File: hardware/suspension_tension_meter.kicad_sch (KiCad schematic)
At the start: 19 parts, among them J1 Goldpin, J2 24V, J3 CAN, U1 STM32L4P5RET6, Y1 TBD

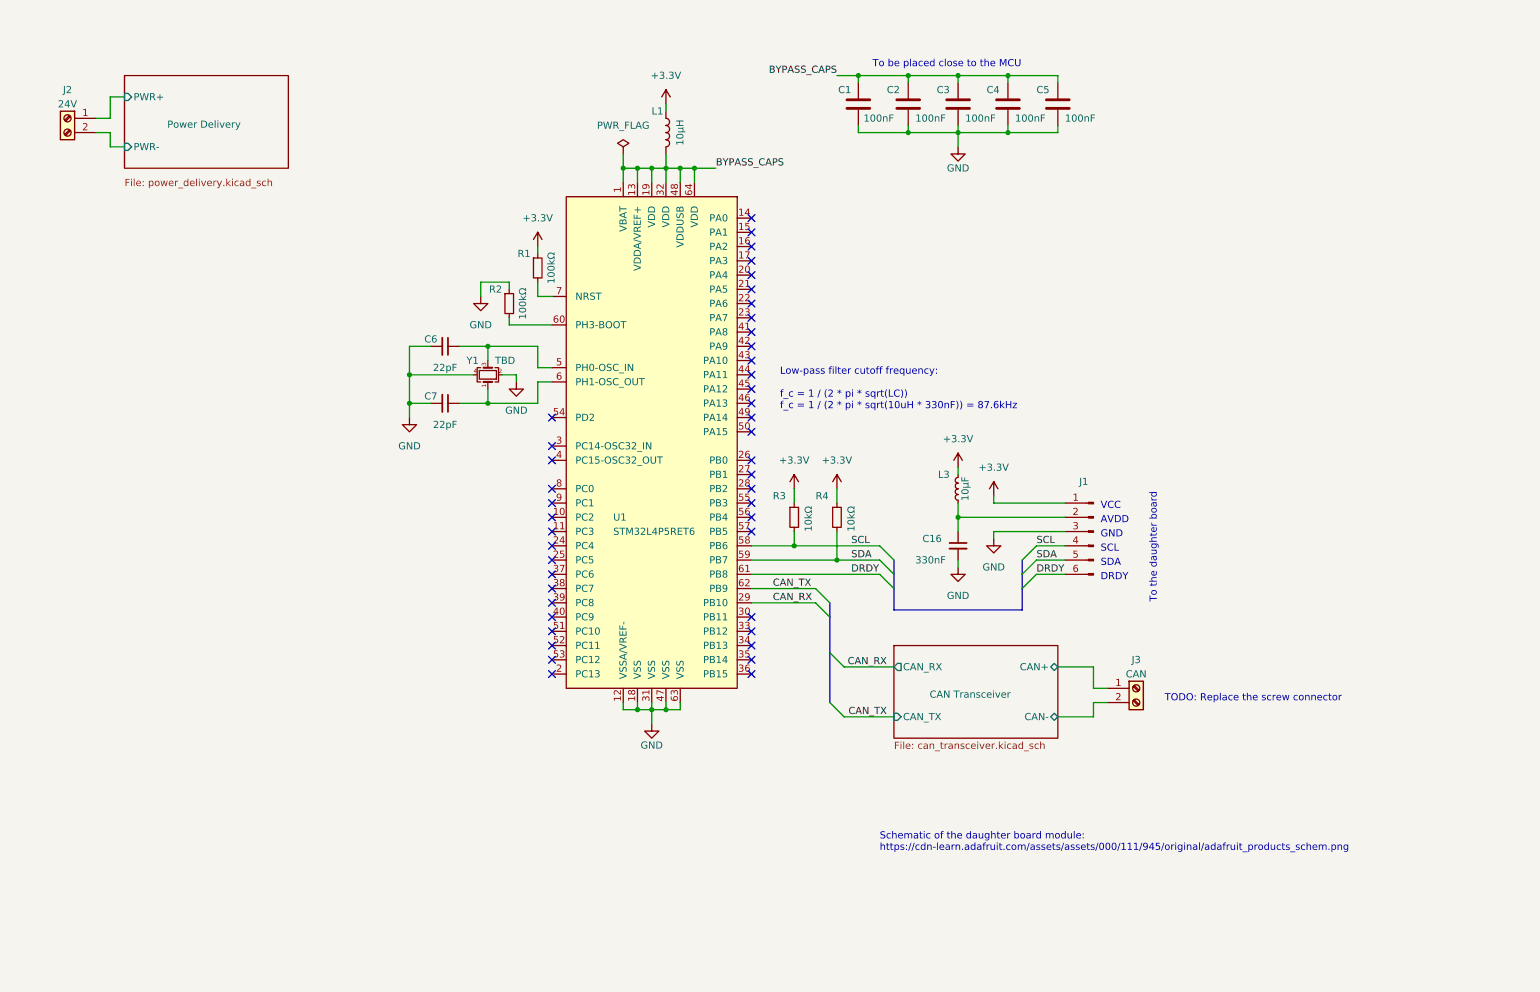
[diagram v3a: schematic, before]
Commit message: Refactor the main sheet
- Replace screw connectors with a goldpin header
- Add reset button
- Add SWD debugger header
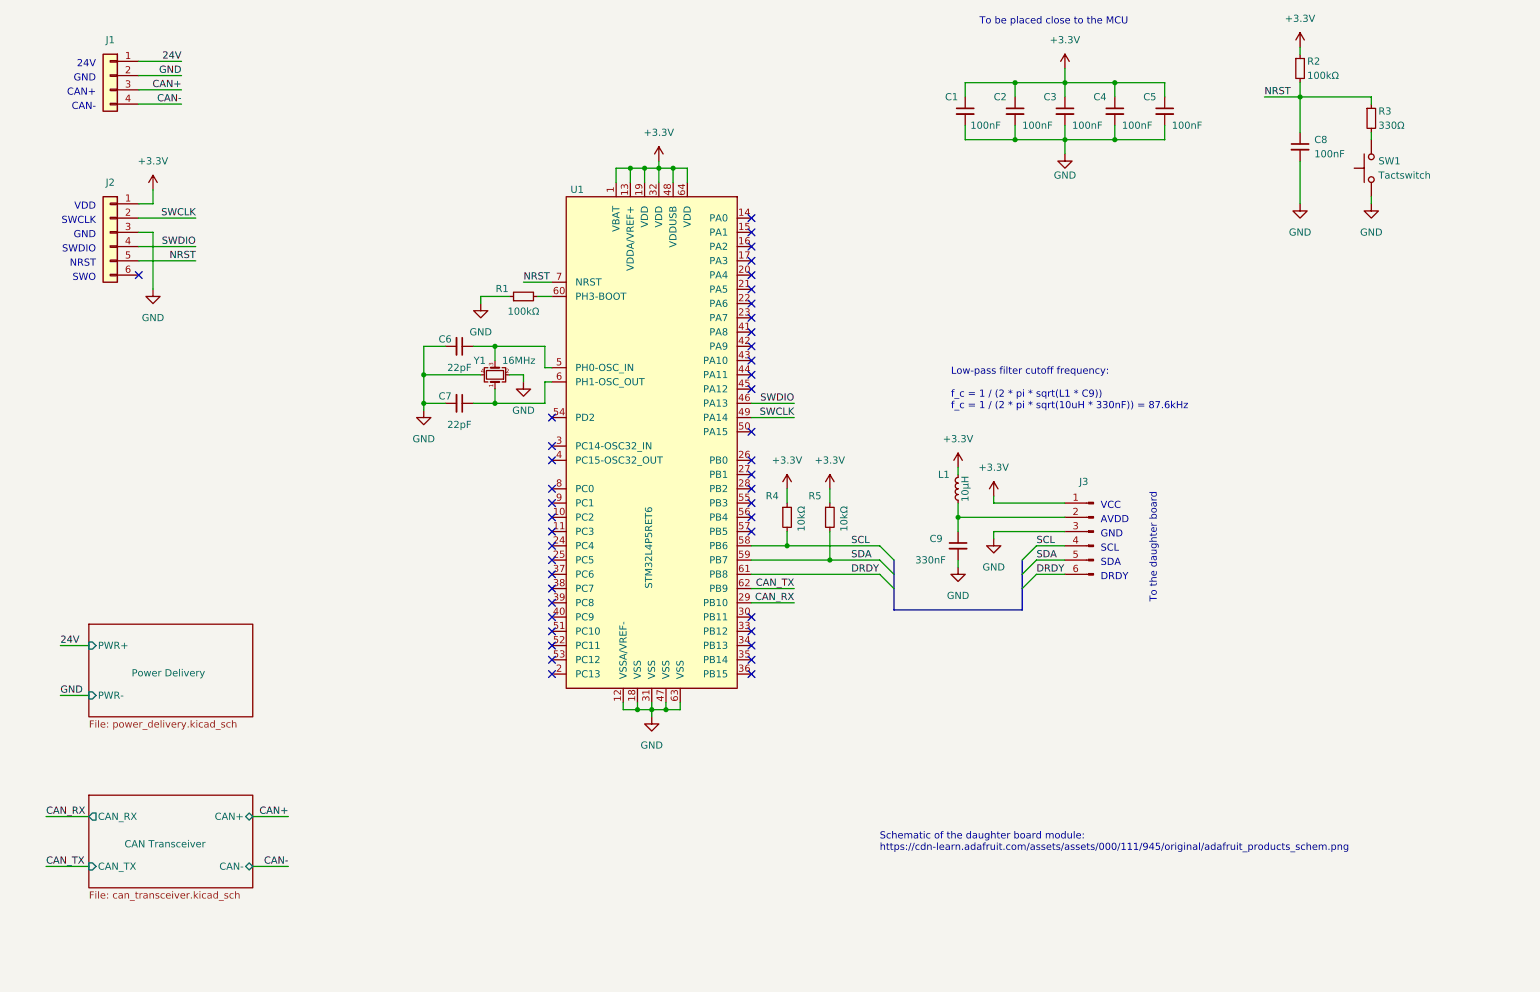
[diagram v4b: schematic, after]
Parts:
- removed J2: 24V, symbol Connector:Screw_Terminal_01x02
- removed J3: CAN, symbol Connector:Screw_Terminal_01x02
- removed L1: 10μH, Inductor_SMD:L_0805_2012Metric, symbol Device:L
- removed R1: 100kΩ, Resistor_SMD:R_0603_1608Metric, symbol Device:R_Small
- added C8: 100nF, symbol Device:C_Small
- added J1: Conn_01x04, symbol Connector_Generic:Conn_01x04
- added J2: Conn_01x06, symbol Connector_Generic:Conn_01x06
- added R2: 100kΩ, symbol Device:R_Small
- added R3: 330Ω, symbol Device:R_Small
- added SW1: Tactswitch, symbol Switch:SW_Push
- C1, C2, C3, C4, C5: symbol Device:C -> Device:C_Small
- L1: renamed from L3; value 10μF -> 10μH
- Y1: value TBD -> 16MHz
- renumbered C16 to C9, J1 to J3, R2 to R1, R3 to R4, R4 to R5
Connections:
- net BYPASS_CAPS is gone; now on net +3.3V: C1.1, C2.1, C3.1, C4.1, C5.1, U1.1 (VBAT), U1.13 (VDDA/VREF+), U1.19 (VDD), U1.32 (VDD), U1.48 (VDDUSB), U1.64 (VDD)
- net +3.3V: now also J2.1 (Pin_1), R2.1
- net GND: now also C8.2, J1.2 (Pin_2), J2.3 (Pin_3), SW1.1
- net SWDIO: now reaches U1.46 (PA13)
- net SWDIO: now also J2.4 (Pin_4)
- net SWCLK: now reaches U1.49 (PA14)
- net SWCLK: now also J2.2 (Pin_2)
- net NRST: now reaches U1.7 (NRST)
- net NRST: now also C8.1, J2.5 (Pin_5), R2.2, R3.1
- new net: R3.2, SW1.2
- new net 24V: J1.1 (Pin_1)
- new net CAN+: J1.3 (Pin_3)
- new net CAN-: J1.4 (Pin_4)
- no-connect marks 44 -> 43
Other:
- note added: "24V"
- note added: "CAN+"
- note added: "CAN-"
- note added: "Low-pass filter cutoff frequency: f_c = 1 / (2 * pi * sqrt(L1 * C9)) f_c = 1 / (2 * pi * sqrt(10uH * 330nF)) = 87.6kHz"
- note added: "NRST"
- note added: "SWCLK"
- note added: "SWDIO"
- note added: "SWO"
- note added: "VDD"
- note removed: "Low-pass filter cutoff frequency: f_c = 1 / (2 * pi * sqrt(LC)) f_c = 1 / (2 * pi * sqrt(10uH * 330nF)) = 87.6kHz"
- note removed: "TODO: Replace the screw connector"
- moved on the sheet: C1, C2, C3, C4, C5, C6, C7, R1, R4, R5, Y1

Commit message: Add ADC circuit
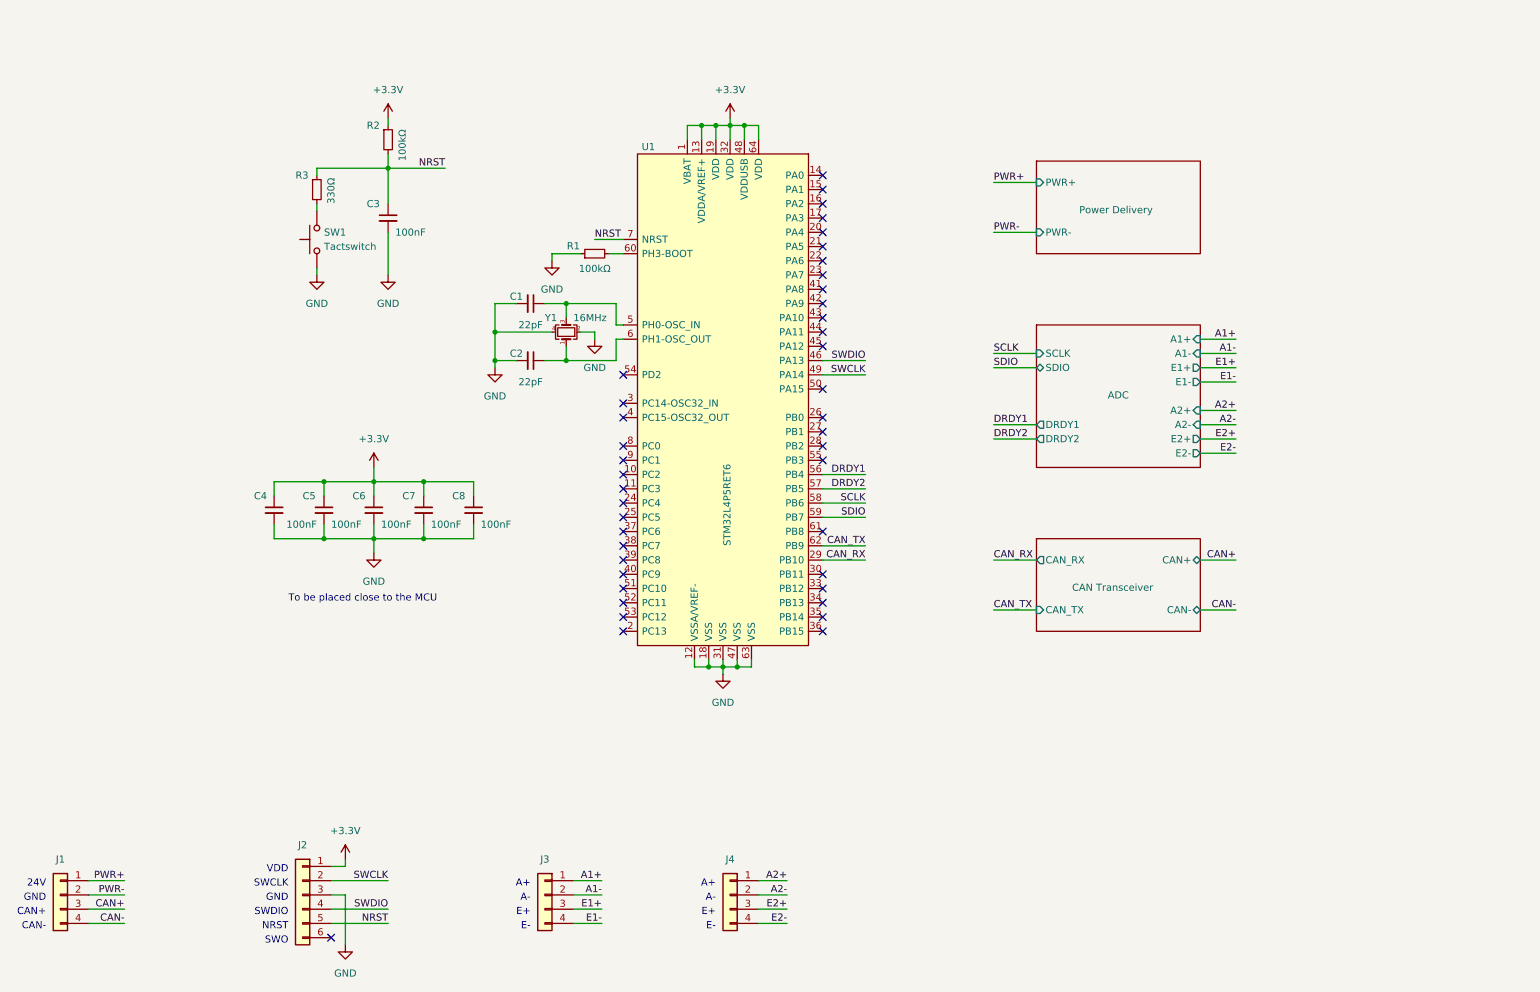
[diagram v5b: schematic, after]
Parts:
- removed C9: 330nF, symbol Device:C_Small
- removed J3: Goldpin, symbol Connector:Conn_01x06_Male
- removed L1: 10μH, symbol Device:L_Small
- removed R4, R5: 10kΩ, symbol Device:R_Small
- added J3, J4: Conn_01x04, symbol Connector_Generic:Conn_01x04
- U1: symbol Local_Library:STM32L4P5RET6-STM32L4P5RET6 -> Local_Library:STM32L4P5RET6
- renumbered C6 to C1, C7 to C2, C8 to C3, C1 to C4, C2 to C5, C3 to C6, C4 to C7, C5 to C8
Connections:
- net GND: no longer J1.2 (Pin_2)
- net DRDY1: now reaches U1.56 (PB4)
- net DRDY2: now reaches U1.57 (PB5)
- net 24V renamed PWR+
- net DRDY: no longer names the net of U1.61 (PB8)
- net SCL renamed SCLK
- net SDA renamed SDIO
- new net A1+: J3.1 (Pin_1)
- new net A1-: J3.2 (Pin_2)
- new net A2+: J4.1 (Pin_1)
- new net A2-: J4.2 (Pin_2)
- new net E1+: J3.3 (Pin_3)
- new net E1-: J3.4 (Pin_4)
- new net E2+: J4.3 (Pin_3)
- new net E2-: J4.4 (Pin_4)
- new net PWR-: J1.2 (Pin_2)
- no-connect marks 43 -> 42
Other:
- added sheet ADC (adc.kicad_sch)
- note added: "A+"
- note added: "A-"
- note added: "E+"
- note added: "E-"
- note removed: "AVDD"
- note removed: "DRDY"
- note removed: "Low-pass filter cutoff frequency: f_c = 1 / (2 * pi * sqrt(L1 * C9)) f_c = 1 / (2 * pi * sqrt(10uH * 330nF)) = 87.6kHz"
- note removed: "SCL"
- note removed: "SDA"
- note removed: "Schematic of the daughter board module: https://cdn-learn.adafruit.com/assets/assets/000/111/945/original/adafruit_products_schem.png"
- note removed: "To the daughter board"
- note removed: "VCC"
- moved on the sheet: C1, C2, C3, C4, C5, C6, C7, C8, J1, J2, R1, R2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

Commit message: Connect each ADC to a separate I2C bus
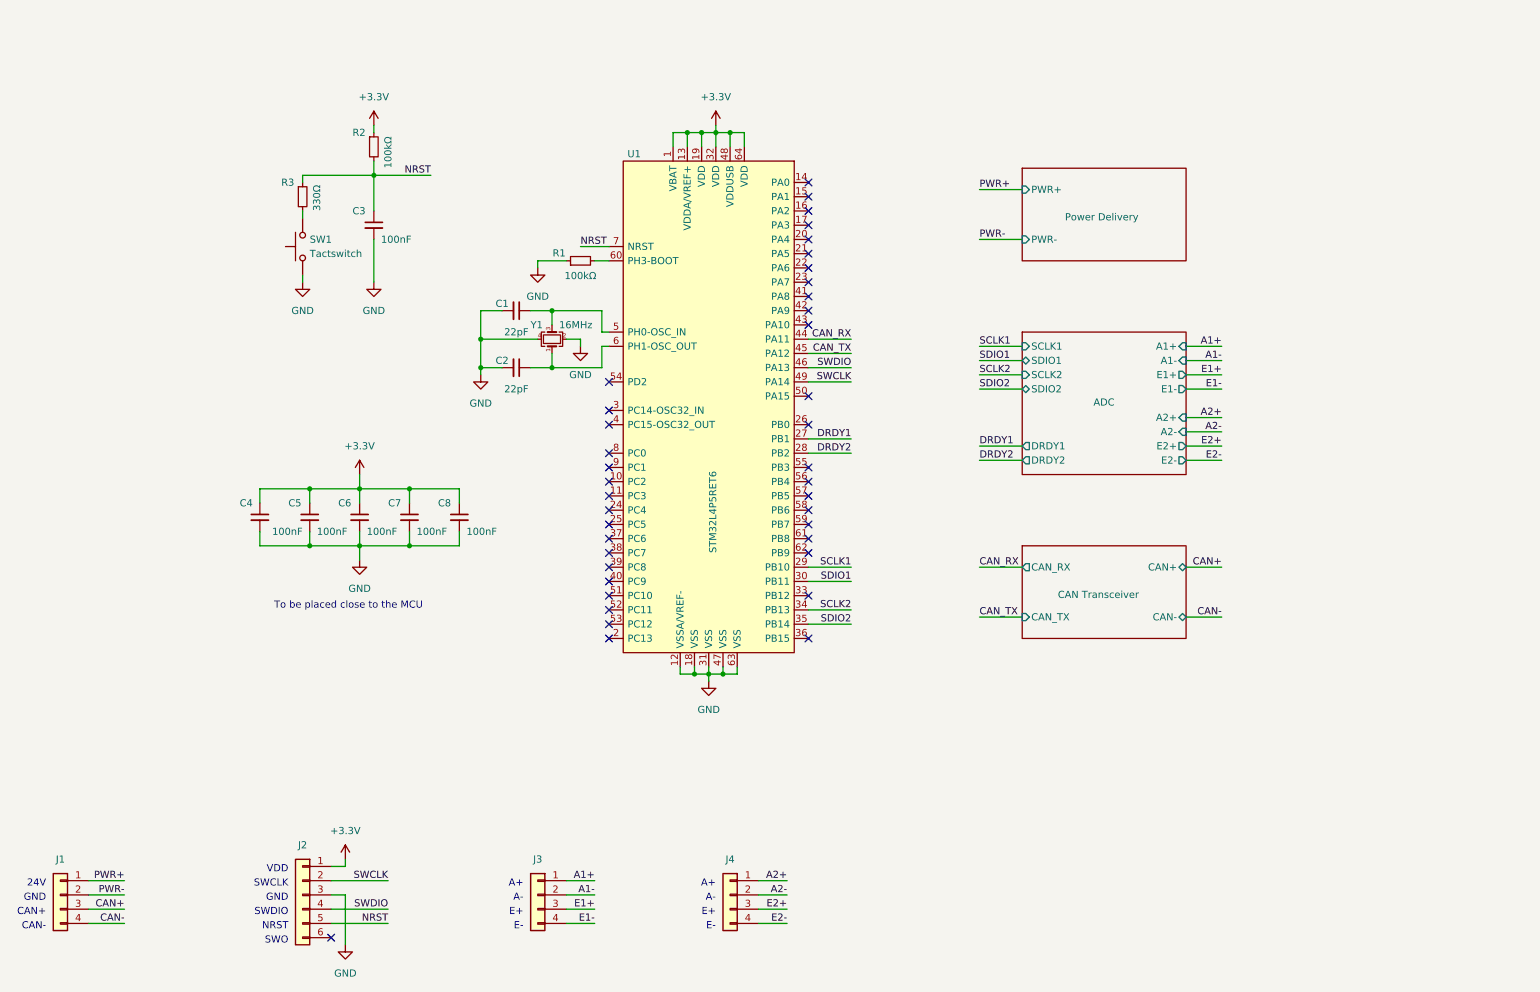
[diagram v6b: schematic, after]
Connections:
- net CAN_RX: now also U1.44 (PA11); no longer U1.29 (PB10)
- net CAN_TX: now also U1.45 (PA12); no longer U1.62 (PB9)
- net DRDY1: now also U1.27 (PB1); no longer U1.56 (PB4)
- net DRDY2: now also U1.28 (PB2); no longer U1.57 (PB5)
- net SDIO1: now reaches U1.30 (PB11)
- net SCLK2: now reaches U1.34 (PB13)
- net SDIO2: now reaches U1.35 (PB14)
- net SCLK: no longer names the net of U1.58 (PB6)
- net SDIO: no longer names the net of U1.59 (PB7)
- new net SCLK1: U1.29 (PB10)
- no-connect marks 42 -> 40
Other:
- sheet ADC ports: added SCLK1, SCLK2, SDIO1, SDIO2; removed SCLK, SDIO
- moved on the sheet: C1, C2, C3, C4, C5, C6, C7, C8, J3, R1, R2, R3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

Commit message: Assign footprints to symbols
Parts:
- C3: footprint (none) -> Capacitor_SMD:C_0603_1608Metric
- J1, J3, J4: footprint (none) -> Connector_PinHeader_1.00mm:PinHeader_1x04_P1.00mm_Vertical_SMD_Pin1Left
- J2: footprint (none) -> Connector_PinHeader_1.00mm:PinHeader_1x06_P1.00mm_Vertical_SMD_Pin1Left
- R2, R3: footprint (none) -> Resistor_SMD:R_0603_1608Metric
- SW1: footprint (none) -> Button_Switch_SMD:SW_Push_1P1T_NO_6x6mm_H9.5mm
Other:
- sheet Power Delivery renamed Power Supply
- sheet CAN Transceiver: file can_transceiver.kicad_sch -> can.kicad_sch
- sheet Power Supply: file power_delivery.kicad_sch -> power.kicad_sch

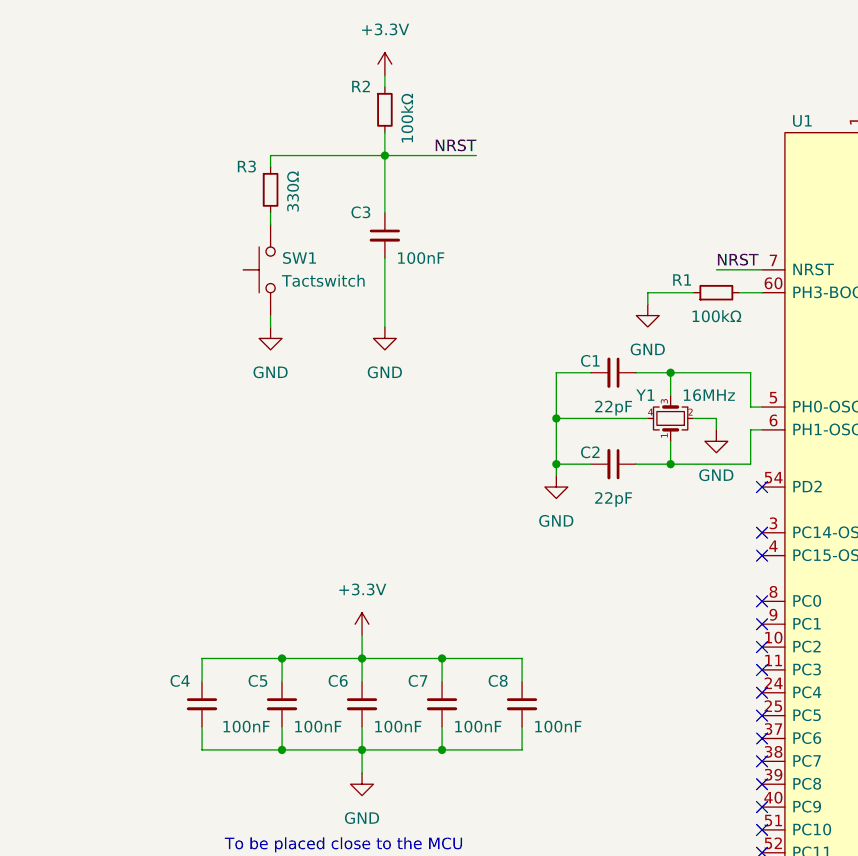
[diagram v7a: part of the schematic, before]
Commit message: Use more efficient buck converter
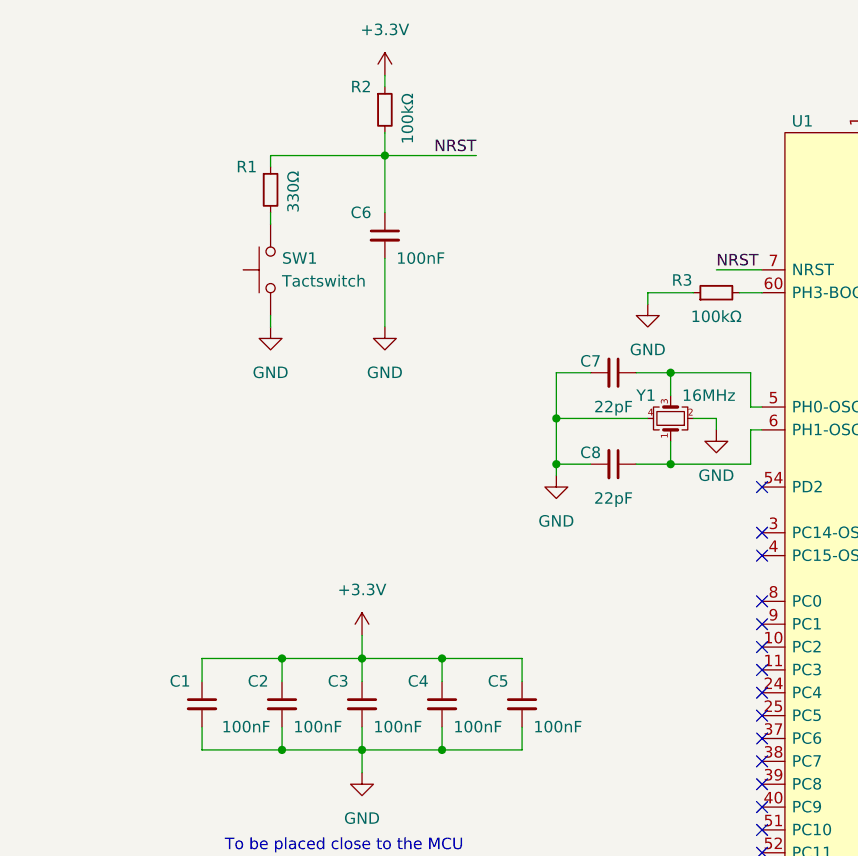
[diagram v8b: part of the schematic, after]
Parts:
- renumbered C4 to C1, C5 to C2, C6 to C3, C7 to C4, C8 to C5, C3 to C6, C1 to C7, C2 to C8, R3 to R1, R1 to R3
